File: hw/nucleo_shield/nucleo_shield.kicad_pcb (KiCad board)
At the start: 2 copper layers, 150.1 x 80.1 mm, 43 parts, among them CN101 Nucleo-F411RE-CN10, CN71 Nucleo-F411RE-CN7, P1 CONN_INH1, P10 CONN_OUTH1, P11 CONN_OUTH2, P2 CONN_OUT2, P3 CONN_OUT1, P4 POWER_CON, P5 CONN_INH2, P6 ETH_CONN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

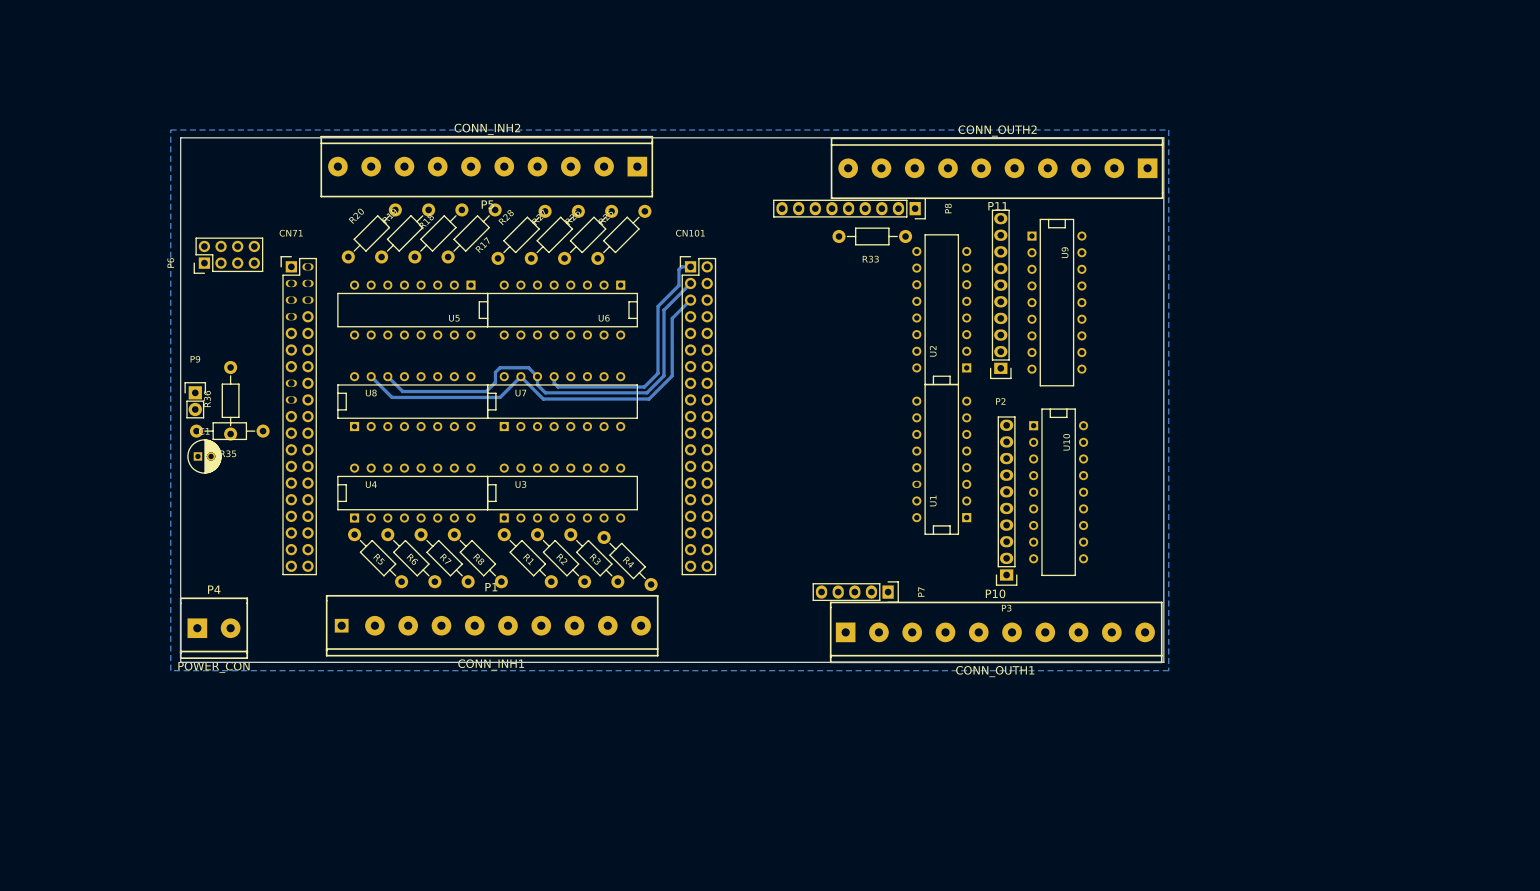
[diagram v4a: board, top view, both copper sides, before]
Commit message: Nucleo: add RS485 headers, add CMS pulldown  resistors
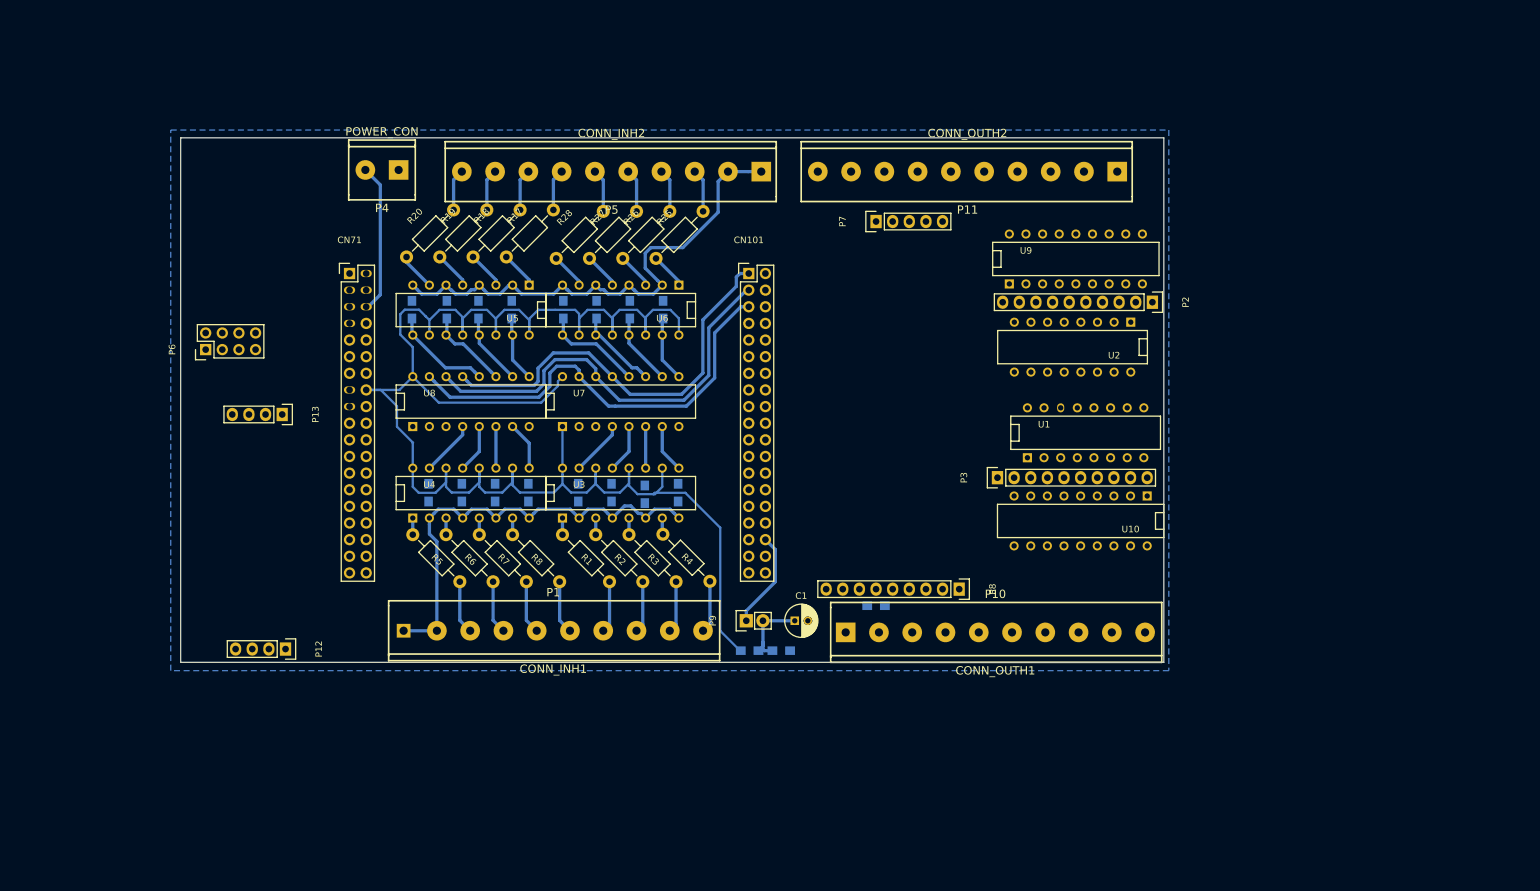
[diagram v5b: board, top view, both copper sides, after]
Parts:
- added P12: CONN_RS485_OUT, Pin_Headers:Pin_Header_Straight_1x04, F.Cu at (111.5, 146.6)
- added P13: CONN_RS485_IN, Pin_Headers:Pin_Header_Straight_1x04, F.Cu at (111.0, 110.7)
- added R10: R, Resistors_SMD:R_0805_HandSoldering, B.Cu at (148.6, 122.7)
- added R11: R, Resistors_SMD:R_0805_HandSoldering, B.Cu at (130.8, 94.7)
- added R12: R, Resistors_SMD:R_0805_HandSoldering, B.Cu at (166.4, 122.9)
- added R13: R, Resistors_SMD:R_0805_HandSoldering, B.Cu at (143.5, 122.7)
- added R14: R, Resistors_SMD:R_0805_HandSoldering, B.Cu at (136.1, 94.7)
- added R15: R, Resistors_SMD:R_0805_HandSoldering, B.Cu at (161.3, 122.7)
- added R16: R, Resistors_SMD:R_0805_HandSoldering, B.Cu at (138.4, 122.7)
- added R21: R, Resistors_SMD:R_0805_HandSoldering, B.Cu at (141.0, 94.7)
- added R22: R, Resistors_SMD:R_0805_HandSoldering, B.Cu at (156.2, 122.7)
- added R23: R, Resistors_SMD:R_0805_HandSoldering, B.Cu at (133.3, 122.7)
- added R24: R, Resistors_SMD:R_0805_HandSoldering, B.Cu at (146.1, 94.7)
- added R29: R, Resistors_SMD:R_0805_HandSoldering, B.Cu at (153.9, 94.7)
- added R30: R, Resistors_SMD:R_0805_HandSoldering, B.Cu at (159.0, 94.7)
- added R31: R, Resistors_SMD:R_0805_HandSoldering, B.Cu at (164.1, 94.7)
- added R32: R, Resistors_SMD:R_0805_HandSoldering, B.Cu at (169.2, 94.7)
- added R9: R, Resistors_SMD:R_0805_HandSoldering, B.Cu at (171.4, 122.7)
- R33, R35, R36: footprint Resistors_ThroughHole:Resistor_Horizontal_RM10mm -> Resistors_SMD:R_0805_HandSoldering; moved to B.Cu
- moved C1 94.5 mm to (189.3, 142.2)
- moved R36 92.3 mm to (187.2, 146.8), turned to 0 degrees
- moved P9 91.0 mm to (181.9, 142.2), turned to 90 degrees
- moved R35 86.2 mm to (182.4, 146.8), turned to 0 degrees
- moved P4 74.5 mm to (126.2, 73.4), turned to 180 degrees
- moved P8 58.5 mm to (214.4, 137.4)
- moved P7 56.6 mm to (201.7, 81.3), turned to 90 degrees
- moved R33 56.6 mm to (201.7, 140.0)
- moved P2 25.3 mm to (243.9, 93.6), turned to 270 degrees
- moved U1 22.3 mm to (233.7, 113.5), turned to 0 degrees
- moved U2 20.8 mm to (231.7, 100.5), turned to 180 degrees
- moved P5 18.9 mm to (161.3, 73.7)
- moved P3 14.9 mm to (220.2, 120.4), turned to 90 degrees
- moved P6 13.2 mm to (99.3, 100.8)
- moved P1 9.49 mm to (152.4, 143.8)
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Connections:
- CN101 pad 10: (no net) -> Net-(CN101-Pad10)
- CN101 pad 12: (no net) -> Net-(CN101-Pad12)
- CN101 pad 14: (no net) -> Net-(CN101-Pad14)
- CN101 pad 16: (no net) -> Net-(CN101-Pad16)
- CN101 pad 18: (no net) -> Net-(CN101-Pad18)
- CN101 pad 2: (no net) -> Net-(CN101-Pad2)
- CN101 pad 23: (no net) -> Net-(CN101-Pad23)
- CN101 pad 27: (no net) -> Net-(CN101-Pad27)
- CN101 pad 28: (no net) -> Net-(CN101-Pad28)
- CN101 pad 29: (no net) -> Net-(CN101-Pad29)
- CN101 pad 30: (no net) -> Net-(CN101-Pad30)
- CN101 pad 31: (no net) -> Net-(CN101-Pad31)
- CN101 pad 32: (no net) -> Net-(CN101-Pad32)
- CN101 pad 33: (no net) -> Net-(CN101-Pad33)
- CN101 pad 34: (no net) -> SCT_IN
- CN101 pad 35: (no net) -> Net-(CN101-Pad35)
- CN101 pad 36: (no net) -> Net-(CN101-Pad36)
- CN101 pad 37: (no net) -> Net-(CN101-Pad37)
- CN101 pad 38: (no net) -> Net-(CN101-Pad38)
- CN101 pad 4: (no net) -> Net-(CN101-Pad4)
- CN101 pad 6: (no net) -> Net-(CN101-Pad6)
- CN101 pad 7: (no net) -> Net-(CN101-Pad7)
- CN101 pad 8: (no net) -> Net-(CN101-Pad8)
- CN71 pad 10: (no net) -> Net-(CN71-Pad10)
- CN71 pad 11: (no net) -> Net-(CN71-Pad11)
- CN71 pad 12: (no net) -> Net-(CN71-Pad12)
- CN71 pad 13: (no net) -> Net-(CN71-Pad13)
- CN71 pad 14: (no net) -> Net-(CN71-Pad14)
- CN71 pad 15: (no net) -> RS_DE
- CN71 pad 17: (no net) -> RS_RX
- CN71 pad 21: (no net) -> RS_TX
- CN71 pad 23: (no net) -> Net-(CN71-Pad23)
- CN71 pad 24: (no net) -> Net-(CN71-Pad24)
- CN71 pad 25: (no net) -> Net-(CN71-Pad25)
- CN71 pad 26: (no net) -> Net-(CN71-Pad26)
- CN71 pad 27: (no net) -> Net-(CN71-Pad27)
- CN71 pad 28: SCT_IN -> Net-(CN71-Pad28)
- CN71 pad 29: (no net) -> Net-(CN71-Pad29)
- CN71 pad 30: (no net) -> Net-(CN71-Pad30)
- CN71 pad 31: (no net) -> Net-(CN71-Pad31)
- CN71 pad 32: (no net) -> Net-(CN71-Pad32)
- CN71 pad 33: (no net) -> Net-(CN71-Pad33)
- CN71 pad 34: (no net) -> Net-(CN71-Pad34)
- CN71 pad 35: (no net) -> Net-(CN71-Pad35)
- CN71 pad 36: (no net) -> Net-(CN71-Pad36)
- CN71 pad 37: (no net) -> Net-(CN71-Pad37)
- CN71 pad 38: (no net) -> Net-(CN71-Pad38)
- CN71 pad 4: (no net) -> Net-(CN71-Pad4)
- CN71 pad 7: (no net) -> Net-(CN71-Pad7)
- CN71 pad 9: (no net) -> Net-(CN71-Pad9)
- P4 pad 1: +5V -> GND
- P4 pad 2: GND -> +5V
- P6 pad 1: +5V -> GND
- P6 pad 2: GND -> SPI3_MISO
- P6 pad 3: (no net) -> SPI3_MOSI
- P6 pad 4: (no net) -> SPI3_SCK
- P6 pad 5: SPI3_MOSI -> ETH_CS
- P6 pad 6: SPI3_SCK -> ETH_RST
- P6 pad 7: GND -> +5V
- P6 pad 8: SPI3_MISO -> GND
- P7 pad 5: (no net) -> Net-(P7-Pad5)
- U2 pad 9: (no net) -> Net-(U2-Pad9)
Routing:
- net +3V3: track 0.00 -> 265.2 mm
- net GND_24V: track 0.00 -> 146.6 mm
- net IO_INT: track 37.1 -> 63.4 mm
- net +5V: track 0.00 -> 22.9 mm
- net in16: track 0.00 -> 15.4 mm
- net in12: track 0.00 -> 15.4 mm
- net SCT_IN: track 0.00 -> 14.8 mm
- net in11: track 0.00 -> 12.8 mm
- net in15: track 0.00 -> 12.8 mm
- net Net-(C1-Pad1): track 0.00 -> 12.3 mm
- net in14: track 0.00 -> 11.0 mm
- net in10: track 0.00 -> 11.0 mm
- net in9: track 0.00 -> 9.98 mm
- net in13: track 0.00 -> 9.98 mm
- net in1: track 0.00 -> 8.45 mm
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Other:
- net class mini added: clearance 0.1, trace_width 0.35, via_dia 1.3, via_drill 1

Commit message: Nucleo: Rework connection
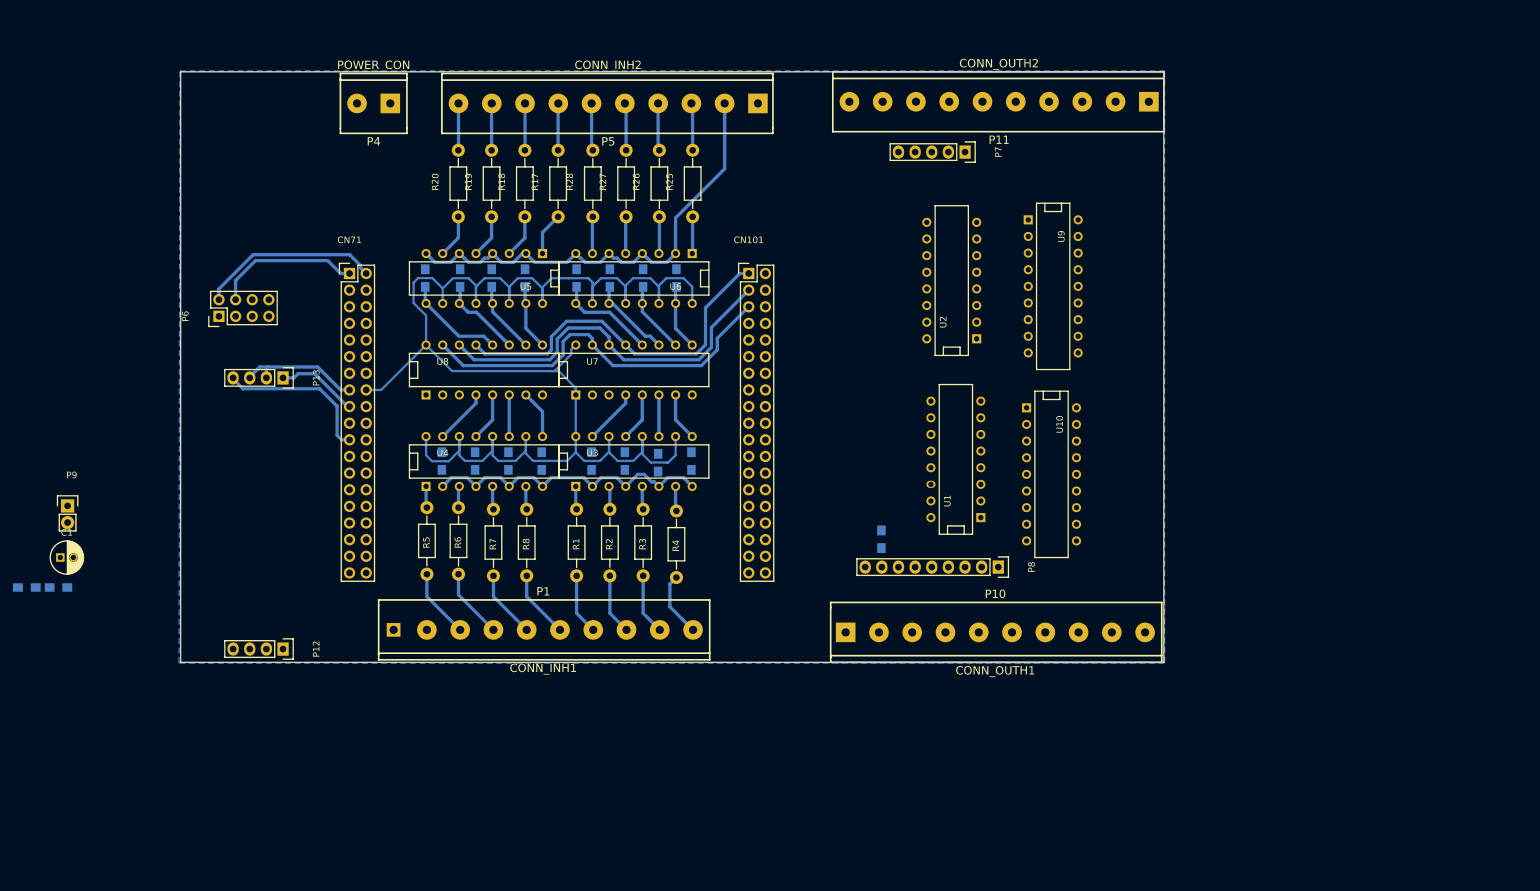
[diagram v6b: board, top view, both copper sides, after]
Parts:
- removed P2: CONN_OUT2, Pin_Headers:Pin_Header_Straight_1x10
- removed P3: CONN_OUT1, Pin_Headers:Pin_Header_Straight_1x10
- moved C1 112.6 mm to (77.1, 132.6)
- moved R35 110.8 mm to (72.0, 137.2)
- moved R36 110.8 mm to (76.8, 137.2)
- moved P9 105.1 mm to (78.2, 124.7), turned to 0 degrees
- moved U2 21.1 mm to (213.2, 90.3), turned to 90 degrees
- moved U1 20.2 mm to (213.9, 117.6), turned to 90 degrees
- moved P7 17.2 mm to (215.3, 70.7), turned to 270 degrees
- moved P11 11.7 mm to (220.5, 63.0)
- moved P5 10.4 mm to (160.8, 63.2)
- moved P4 10.2 mm to (125.0, 63.2)
- moved R33 10.2 mm to (202.5, 129.8), turned to 270 degrees
- moved R17 8.76 mm to (153.1, 75.5), turned to 90 degrees
- moved R19 8.76 mm to (143.0, 75.5), turned to 90 degrees
- moved R18 8.76 mm to (148.1, 75.5), turned to 90 degrees
- moved R20 8.76 mm to (137.9, 75.5), turned to 90 degrees
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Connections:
- CN101 pad 10: Net-(CN101-Pad10) -> (no net)
- CN101 pad 11: SPI1_SCK -> (no net)
- CN101 pad 12: Net-(CN101-Pad12) -> SRCLK
- CN101 pad 13: SPI1_MISO -> (no net)
- CN101 pad 14: Net-(CN101-Pad14) -> SRLatch
- CN101 pad 15: SPI1_MOSI -> (no net)
- CN101 pad 16: Net-(CN101-Pad16) -> SRDATA
- CN101 pad 17: SD_CS -> (no net)
- CN101 pad 18: Net-(CN101-Pad18) -> (no net)
- CN101 pad 19: LCD_CS -> (no net)
- CN101 pad 2: Net-(CN101-Pad2) -> SD_CS
- CN101 pad 21: LCD_RST -> (no net)
- CN101 pad 22: SRCLK -> (no net)
- CN101 pad 23: Net-(CN101-Pad23) -> (no net)
- CN101 pad 24: SRLatch -> (no net)
- CN101 pad 25: LCD_DC -> (no net)
- CN101 pad 26: SRDATA -> SPI1_MOSI
- CN101 pad 27: Net-(CN101-Pad27) -> (no net)
- CN101 pad 28: Net-(CN101-Pad28) -> SPI1_MISO
- CN101 pad 29: Net-(CN101-Pad29) -> (no net)
- CN101 pad 30: Net-(CN101-Pad30) -> SPI1_SCK
- CN101 pad 31: Net-(CN101-Pad31) -> (no net)
- CN101 pad 32: Net-(CN101-Pad32) -> (no net)
- CN101 pad 33: Net-(CN101-Pad33) -> LCD_CS
- CN101 pad 35: Net-(CN101-Pad35) -> LCD_RST
- CN101 pad 36: Net-(CN101-Pad36) -> (no net)
- CN101 pad 37: Net-(CN101-Pad37) -> LCD_DC
- CN101 pad 38: Net-(CN101-Pad38) -> (no net)
- CN101 pad 4: Net-(CN101-Pad4) -> (no net)
- CN101 pad 6: Net-(CN101-Pad6) -> (no net)
- CN101 pad 7: Net-(CN101-Pad7) -> (no net)
- CN101 pad 8: Net-(CN101-Pad8) -> (no net)
- CN71 pad 10: Net-(CN71-Pad10) -> (no net)
- CN71 pad 11: Net-(CN71-Pad11) -> (no net)
- CN71 pad 12: Net-(CN71-Pad12) -> (no net)
- CN71 pad 13: Net-(CN71-Pad13) -> ETH_CS
- CN71 pad 14: Net-(CN71-Pad14) -> (no net)
- CN71 pad 23: Net-(CN71-Pad23) -> (no net)
- CN71 pad 24: Net-(CN71-Pad24) -> (no net)
- CN71 pad 25: Net-(CN71-Pad25) -> (no net)
- CN71 pad 26: Net-(CN71-Pad26) -> (no net)
- CN71 pad 27: Net-(CN71-Pad27) -> (no net)
- CN71 pad 28: Net-(CN71-Pad28) -> (no net)
- CN71 pad 29: Net-(CN71-Pad29) -> (no net)
- CN71 pad 30: Net-(CN71-Pad30) -> (no net)
- CN71 pad 31: Net-(CN71-Pad31) -> (no net)
- CN71 pad 32: Net-(CN71-Pad32) -> (no net)
- CN71 pad 33: Net-(CN71-Pad33) -> (no net)
- CN71 pad 34: Net-(CN71-Pad34) -> (no net)
- CN71 pad 35: Net-(CN71-Pad35) -> (no net)
- CN71 pad 36: Net-(CN71-Pad36) -> (no net)
- CN71 pad 37: Net-(CN71-Pad37) -> (no net)
- CN71 pad 38: Net-(CN71-Pad38) -> (no net)
- CN71 pad 4: Net-(CN71-Pad4) -> ETH_RST
- CN71 pad 7: Net-(CN71-Pad7) -> (no net)
- CN71 pad 9: Net-(CN71-Pad9) -> (no net)
- P12 pad 2: Net-(P12-Pad2) -> (no net)
- P12 pad 3: Net-(P12-Pad3) -> (no net)
- P7 pad 5: Net-(P7-Pad5) -> (no net)
- U2 pad 9: Net-(U2-Pad9) -> (no net)
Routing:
- net +3V3: track 265.2 -> 226.4 mm
- net GND_24V: track 146.6 -> 118.3 mm
- net SPI3_MISO: track 0.00 -> 27.7 mm
- net RS_TX: track 0.00 -> 24.4 mm
- net +5V: track 22.9 -> 0.00 mm
- net SPI3_SCK: track 0.00 -> 22.4 mm
- net RS_DE: track 0.00 -> 19.2 mm
- net SCT_IN: track 14.8 -> 0.00 mm
- net RS_RX: track 0.00 -> 12.5 mm
- net Net-(C1-Pad1): track 12.3 -> 0.00 mm
- net I2C1_SDA: track 66.6 -> 58.5 mm
- net IO_INT: track 63.4 -> 55.9 mm
- net I2C1_SCL: track 64.9 -> 57.6 mm
- net inh6: track 8.14 -> 10.7 mm
- net inh5: track 8.14 -> 10.6 mm
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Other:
- board size 150.1 x 80.1 mm -> 150.1 x 90.2 mm

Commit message: Add one more shift register
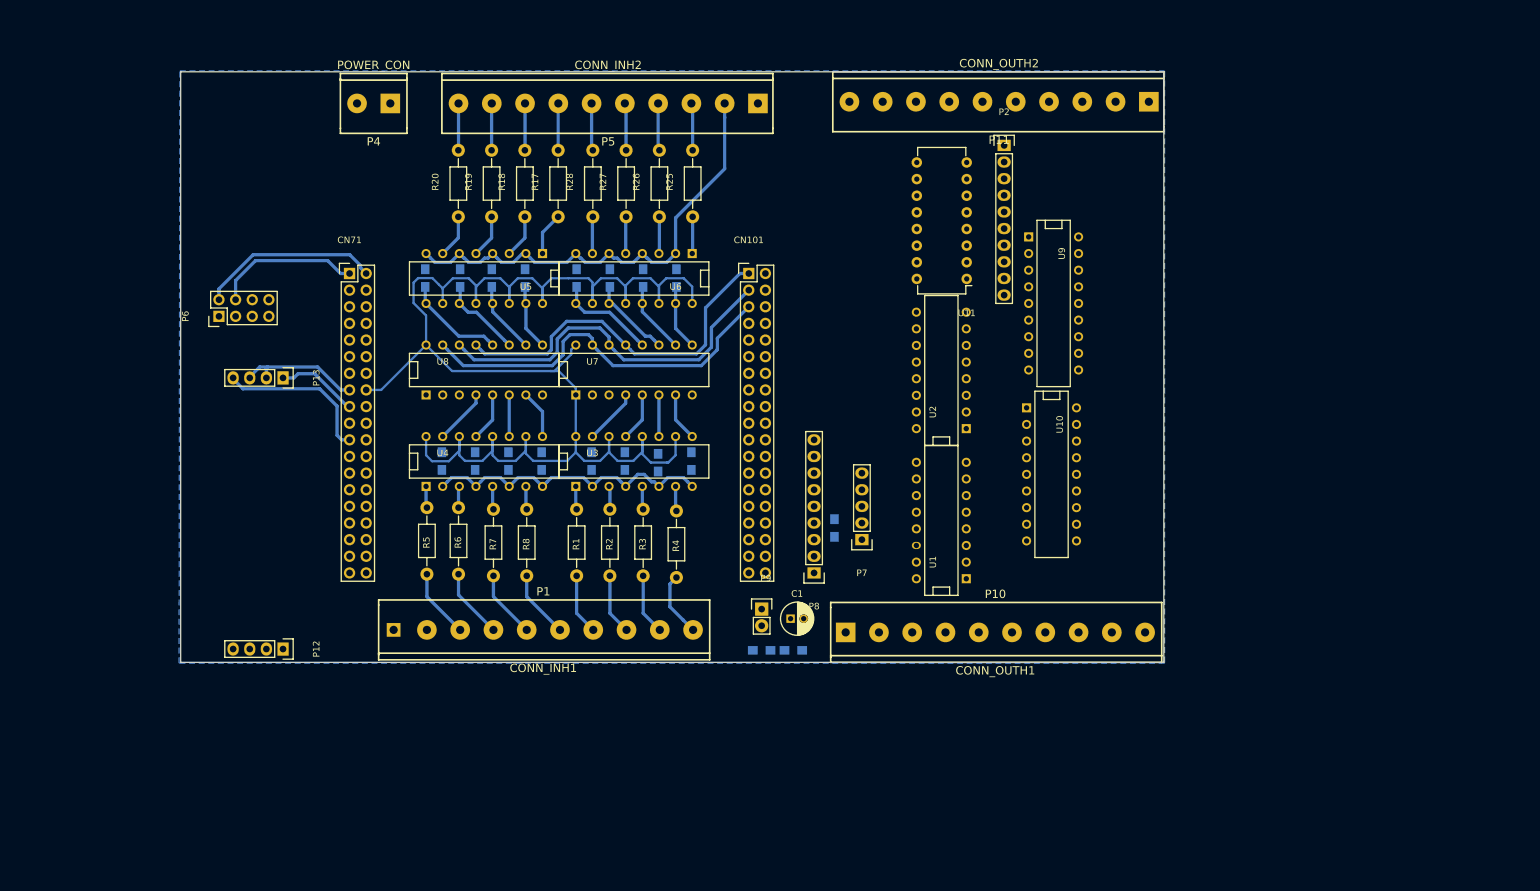
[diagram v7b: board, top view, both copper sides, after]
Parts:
- added P2: CONN_OUT3, Pin_Headers:Pin_Header_Straight_1x10, F.Cu at (221.2, 69.7)
- added U11: 74HC595, Housings_DIP:DIP-16_W7.62mm, F.Cu at (215.5, 90.0)
- moved R35 112.6 mm to (184.2, 146.7)
- moved R36 112.6 mm to (189.0, 146.7)
- moved C1 111.9 mm to (188.6, 141.9)
- moved P9 107.1 mm to (184.2, 140.5)
- moved P7 61.2 mm to (199.5, 129.9), turned to 180 degrees
- moved P8 28.1 mm to (192.2, 134.9), turned to 180 degrees
- moved U2 13.8 mm to (211.6, 104.0)
- moved U1 9.60 mm to (211.6, 126.9)
- moved R33 7.38 mm to (195.3, 128.1), turned to 90 degrees
- moved U9 2.60 mm to (228.8, 93.8)
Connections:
- U2 pad 9: (no net) -> Net-(U11-Pad14)
